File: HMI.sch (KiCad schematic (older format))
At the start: 48 parts, among them J34 Display, J35 SPI Interface, J36 I2C Interface, J37 LED4, J38 LED3, J39 Key 3, J40 Key 4, J41 Key 1, J42 Key 2, J43 Encoder, Q18 2N7002K, Q19 2N7002K, U11 74HC245

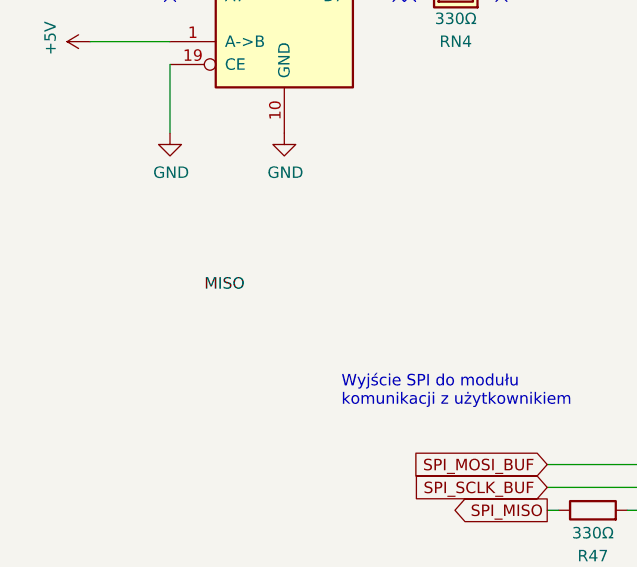
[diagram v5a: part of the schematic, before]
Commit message: Test points, start power plane routing, little change on schematic
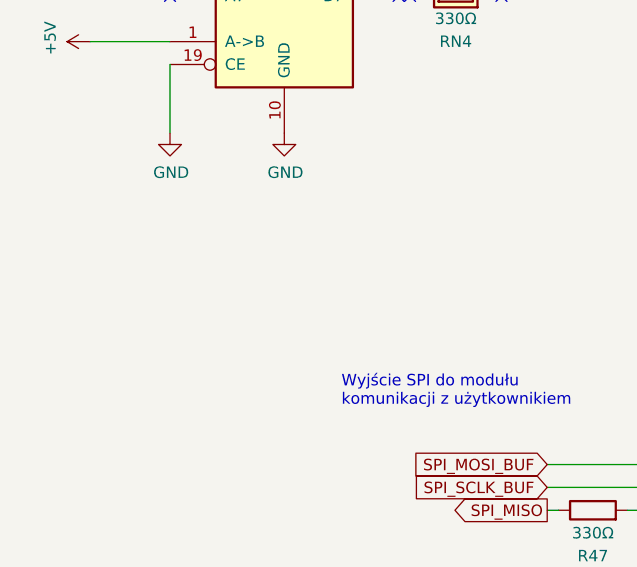
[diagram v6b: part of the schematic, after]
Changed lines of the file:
@@
 Wire Wire Line
 	3850 4700 3850 4900
-Text Label 1750 3650 0    50   ~ 0
-MISO
 $Comp
 L power:GND #PWR?

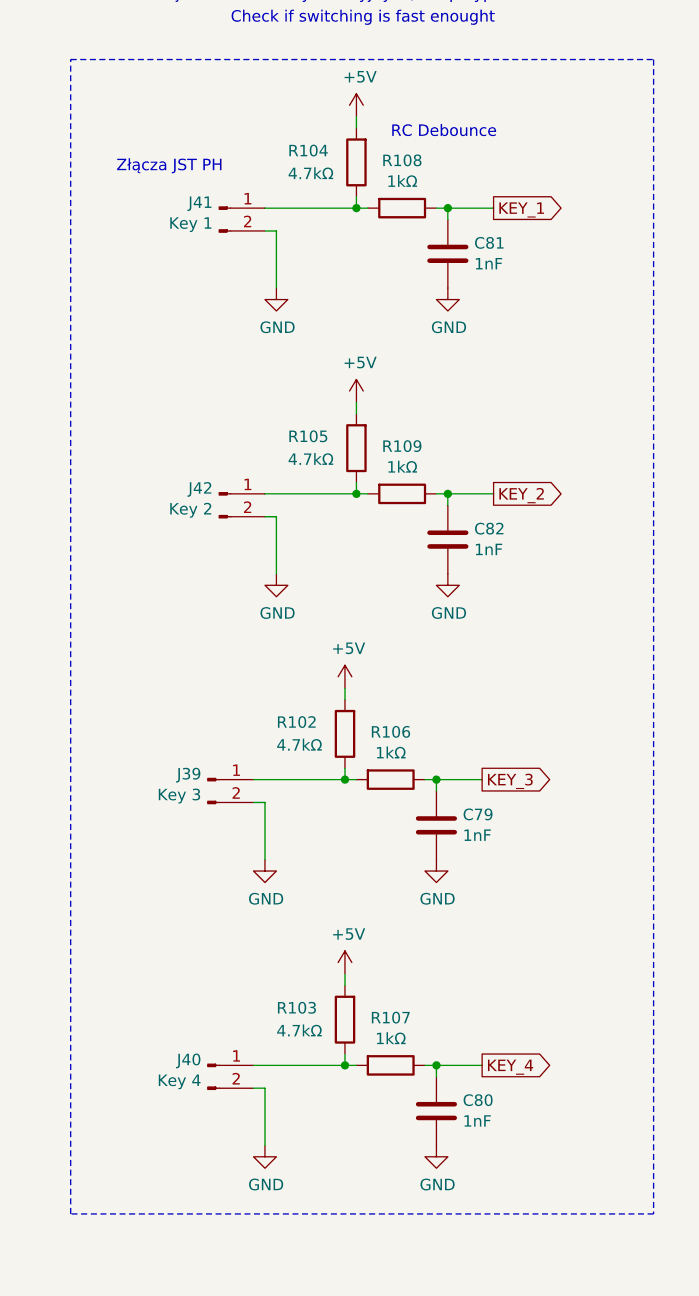
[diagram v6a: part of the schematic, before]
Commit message: Update elements value
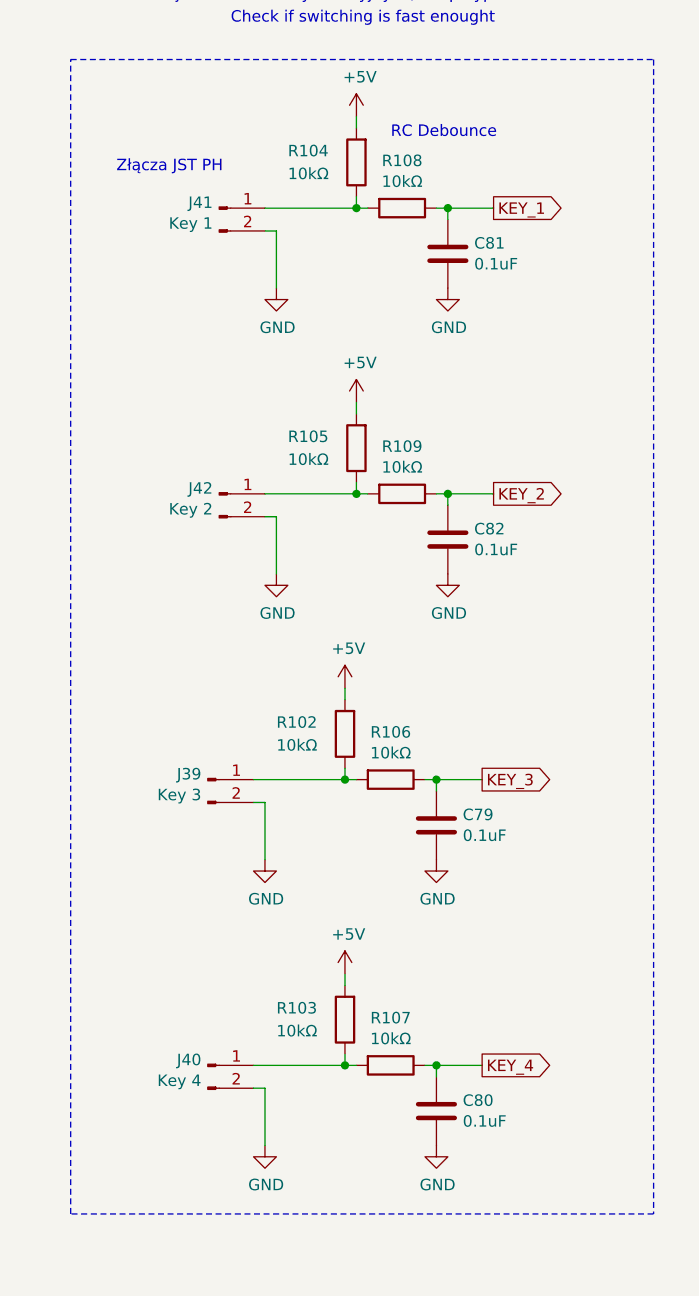
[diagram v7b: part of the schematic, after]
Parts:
- C79, C80, C81, C82: value 1nF -> 0.1uF
- R102, R103, R104, R105: value 4.7kΩ -> 10kΩ
- R106, R107, R108, R109: value 1kΩ -> 10kΩ
- R98, R99: Cena (none) -> 0.03185; Link (none) -> https://www.tme.eu/pl/details/smd0603-100r-1%25/rezystory-s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; Model (none) -> 0603SAF1000T5E; Opis (none) -> Rezystor: thick film; SMD; 0603; 100Ω; 0,1W; ±1%; -55÷155°C; Producent (none) -> ROYAL OHM; Typ (none) -> SMD
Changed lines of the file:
@@
 AR Path="/5E91D96F/5E1B03B6" Ref="C81"  Part="1"
 F 0 "C81" H 10015 1896 50  0000 L CNN
-F 1 "1nF" H 10015 1805 50  0000 L CNN
+F 1 "0.1uF" H 10015 1805 50  0000 L CNN
 F 2 "Capacitor_SMD:C_0603_1608Metric" H 9938 1700 50  0001 C CNN
 F 3 "~" H 9900 1850 50  0001 C CNN
@@
 AR Path="/5E91D96F/5E1B03BC" Ref="R104"  Part="1"
 F 0 "R104" H 9800 1400 50  0000 R CNN
-F 1 "4.7kΩ" H 9800 1500 50  0000 R CNN
+F 1 "10kΩ" H 9800 1500 50  0000 R CNN
 F 2 "Resistor_SMD:R_0603_1608Metric" V 9430 1450 50  0001 C CNN
 F 3 "~" H 9500 1450 50  0001 C CNN
@@
 AR Path="/5E91D96F/5E1B03C2" Ref="R108"  Part="1"
 F 0 "R108" V 9493 1650 50  0000 C CNN
-F 1 "1kΩ" V 9584 1650 50  0000 C CNN
+F 1 "10kΩ" V 9584 1650 50  0000 C CNN
 F 2 "Resistor_SMD:R_0603_1608Metric" V 9630 1650 50  0001 C CNN
 F 3 "~" H 9700 1650 50  0001 C CNN
@@
 AR Path="/5E91D96F/5E1B03E5" Ref="C82"  Part="1"
 F 0 "C82" H 10015 3146 50  0000 L CNN
-F 1 "1nF" H 10015 3055 50  0000 L CNN
+F 1 "0.1uF" H 10015 3055 50  0000 L CNN
 F 2 "Capacitor_SMD:C_0603_1608Metric" H 9938 2950 50  0001 C CNN
 F 3 "~" H 9900 3100 50  0001 C CNN
@@
 AR Path="/5E91D96F/5E1B03EB" Ref="R105"  Part="1"
 F 0 "R105" H 9800 2650 50  0000 R CNN
-F 1 "4.7kΩ" H 9800 2750 50  0000 R CNN
+F 1 "10kΩ" H 9800 2750 50  0000 R CNN
 F 2 "Resistor_SMD:R_0603_1608Metric" V 9430 2700 50  0001 C CNN
 F 3 "~" H 9500 2700 50  0001 C CNN
@@
 AR Path="/5E91D96F/5E1B03F1" Ref="R109"  Part="1"
 F 0 "R109" V 9493 2900 50  0000 C CNN
-F 1 "1kΩ" V 9584 2900 50  0000 C CNN
+F 1 "10kΩ" V 9584 2900 50  0000 C CNN
 F 2 "Resistor_SMD:R_0603_1608Metric" V 9630 2900 50  0001 C CNN
 F 3 "~" H 9700 2900 50  0001 C CNN
@@
 AR Path="/5E91D96F/5E1B0414" Ref="C79"  Part="1"
 F 0 "C79" H 9965 4396 50  0000 L CNN
-F 1 "1nF" H 9965 4305 50  0000 L CNN
+F 1 "0.1uF" H 9965 4305 50  0000 L CNN
 F 2 "Capacitor_SMD:C_0603_1608Metric" H 9888 4200 50  0001 C CNN
 F 3 "~" H 9850 4350 50  0001 C CNN
@@
 AR Path="/5E91D96F/5E1B041A" Ref="R102"  Part="1"
 F 0 "R102" H 9750 3900 50  0000 R CNN
-F 1 "4.7kΩ" H 9750 4000 50  0000 R CNN
+F 1 "10kΩ" H 9750 4000 50  0000 R CNN
 F 2 "Resistor_SMD:R_0603_1608Metric" V 9380 3950 50  0001 C CNN
 F 3 "~" H 9450 3950 50  0001 C CNN
@@
 AR Path="/5E91D96F/5E1B0420" Ref="R106"  Part="1"
 F 0 "R106" V 9443 4150 50  0000 C CNN
-F 1 "1kΩ" V 9534 4150 50  0000 C CNN
+F 1 "10kΩ" V 9534 4150 50  0000 C CNN
 F 2 "Resistor_SMD:R_0603_1608Metric" V 9580 4150 50  0001 C CNN
 F 3 "~" H 9650 4150 50  0001 C CNN
@@
 AR Path="/5E91D96F/5E1B0443" Ref="C80"  Part="1"
 F 0 "C80" H 9965 5646 50  0000 L CNN
-F 1 "1nF" H 9965 5555 50  0000 L CNN
+F 1 "0.1uF" H 9965 5555 50  0000 L CNN
 F 2 "Capacitor_SMD:C_0603_1608Metric" H 9888 5450 50  0001 C CNN
 F 3 "~" H 9850 5600 50  0001 C CNN
@@
 AR Path="/5E91D96F/5E1B0449" Ref="R103"  Part="1"
 F 0 "R103" H 9750 5150 50  0000 R CNN
-F 1 "4.7kΩ" H 9750 5250 50  0000 R CNN
+F 1 "10kΩ" H 9750 5250 50  0000 R CNN
 F 2 "Resistor_SMD:R_0603_1608Metric" V 9380 5200 50  0001 C CNN
 F 3 "~" H 9450 5200 50  0001 C CNN
@@
 AR Path="/5E91D96F/5E1B044F" Ref="R107"  Part="1"
 F 0 "R107" V 9443 5400 50  0000 C CNN
-F 1 "1kΩ" V 9534 5400 50  0000 C CNN
+F 1 "10kΩ" V 9534 5400 50  0000 C CNN
 F 2 "Resistor_SMD:R_0603_1608Metric" V 9580 5400 50  0001 C CNN
 F 3 "~" H 9650 5400 50  0001 C CNN
@@
 F 2 "Resistor_SMD:R_0603_1608Metric" V 5880 1700 50  0001 C CNN
 F 3 "~" H 5950 1700 50  0001 C CNN
+F 4 "0.03185" H 5950 1700 50  0001 C CNN "Cena"
+F 5 "https://www.tme.eu/pl/details/smd0603-100r-1%25/rezystory-smd-0603/royal-ohm/0603saf1000t5e/" H 5950 1700 50  0001 C CNN "Link"
+F 6 "0603SAF1000T5E" H 5950 1700 50  0001 C CNN "Model"
+F 7 "Rezystor: thick film; SMD; 0603; 100Ω; 0,1W; ±1%; -55÷155°C" H 5950 1700 50  0001 C CNN "Opis"
+F 8 "ROYAL OHM" H 5950 1700 50  0001 C CNN "Producent"
+F 9 "SMD" H 5950 1700 50  0001 C CNN "Typ"
 	1    5950 1700
 	0    -1   -1   0
@@
 F 2 "Resistor_SMD:R_0603_1608Metric" V 5880 2900 50  0001 C CNN
 F 3 "~" H 5950 2900 50  0001 C CNN
+F 4 "0.03185" H 5950 2900 50  0001 C CNN "Cena"
+F 5 "https://www.tme.eu/pl/details/smd0603-100r-1%25/rezystory-smd-0603/royal-ohm/0603saf1000t5e/" H 5950 2900 50  0001 C CNN "Link"
+F 6 "0603SAF1000T5E" H 5950 2900 50  0001 C CNN "Model"
+F 7 "Rezystor: thick film; SMD; 0603; 100Ω; 0,1W; ±1%; -55÷155°C" H 5950 2900 50  0001 C CNN "Opis"
+F 8 "ROYAL OHM" H 5950 2900 50  0001 C CNN "Producent"
+F 9 "SMD" H 5950 2900 50  0001 C CNN "Typ"
 	1    5950 2900
 	0    -1   -1   0

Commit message: Updated BOM on schematics
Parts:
- C78: Cena 0.05982 -> 0.07894; Link (none) -> https://www.tme.eu/pl/details/cl10b104kb8nnnc/kondensatory-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; Model CL10B104KB8NNNC -> CL10B104KB8NNNC; Opis (none) -> Kondensator: ceramiczny; MLCC; 100nF; 50V; X7R; ±10%; SMD; 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
- C79, C80, C81, C82: Cena 0.05563 -> 0.07894; Dielektryk (none) -> X7R; Link https://www.tme.eu/pl/details/cl10b102kb8nnnc/kondensatory-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 -> https://www.tme.eu/pl/details/cl10b104kb8nnnc/kondensatory-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; Model CL10B102KB8NNNC -> CL10B104KB8NNNC; Napięcie (none) -> 50V; Opis Kondensator: ceramiczny; MLCC; 1nF; 50V; X7R; ±10%; SMD; 06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 -> Kondensator: ceramiczny; MLCC; 100nF; 50V; X7R; ±10%; SMD; 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
- C85, C86: Cena 0.05563 -> 0.05269; Dielektryk (none) -> X7R; Link (none) -> https://www.tme.eu/pl/details/vj0603y103kxacw1bc/kondensato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; Model (none) -> VJ0603Y103KXACW1BC; Napięcie (none) -> 50V; Opis (none) -> Kondensator: ceramiczny; MLCC; 10nF; 50V; X7R; ±10%; SMD; 0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; Producent (none) -> VISHAY
- R100, R101, R47: Link (none) -> https://www.tme.eu/pl/details/smd0603-330r-1%25/rezystory-s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; Model (none) -> 0603SAF3300T5E; Opis (none) -> Rezystor: thick film; SMD; 0603; 330Ω; 0,1W; ±1%; -55÷155°C; Producent (none) -> ROYAL OHM
- R96, R97: Cena (none) -> 0.1; Link (none) -> https://www.tme.eu/pl/details/crcw060320r0fktabc/rezystory-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; Model (none) -> CRCW060320R0FKTABC; Opis (none) -> Rezystor: thick film; SMD; 0603; 20Ω; 0,1W; ±1%; -55÷155°C; Producent (none) -> VISHAY
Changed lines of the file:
@@
 F 2 "Capacitor_SMD:C_0603_1608Metric" H 9938 1700 50  0001 C CNN
 F 3 "~" H 9900 1850 50  0001 C CNN
-F 4 "0.05563" H 9900 1850 50  0001 C CNN "Cena"
-F 5 "https://www.tme.eu/pl/details/cl10b102kb8nnnc/kondensatory-mlcc-smd-0603/samsung/" H 9900 1850 50  0001 C CNN "Link"
-F 6 "CL10B102KB8NNNC" H 9900 1850 50  0001 C CNN "Model"
-F 7 "Kondensator: ceramiczny; MLCC; 1nF; 50V; X7R; ±10%; SMD; 0603" H 9900 1850 50  0001 C CNN "Opis"
+F 4 "0.07894" H 9900 1850 50  0001 C CNN "Cena"
+F 5 "https://www.tme.eu/pl/details/cl10b104kb8nnnc/kondensatory-mlcc-smd-0603/samsung/" H 9900 1850 50  0001 C CNN "Link"
+F 6 "CL10B104KB8NNNC" H 9900 1850 50  0001 C CNN "Model"
+F 7 "Kondensator: ceramiczny; MLCC; 100nF; 50V; X7R; ±10%; SMD; 0603" H 9900 1850 50  0001 C CNN "Opis"
 F 8 "SAMSUNG" H 9900 1850 50  0001 C CNN "Producent"
 F 9 "SMD" H 9900 1850 50  0001 C CNN "Typ"
+F 10 "X7R" H 9900 1850 50  0001 C CNN "Dielektryk"
+F 11 "50V" H 9900 1850 50  0001 C CNN "Napięcie"
 	1    9900 1850
 	1    0    0    -1
@@
 F 2 "Capacitor_SMD:C_0603_1608Metric" H 9938 2950 50  0001 C CNN
 F 3 "~" H 9900 3100 50  0001 C CNN
-F 4 "0.05563" H 9900 3100 50  0001 C CNN "Cena"
-F 5 "https://www.tme.eu/pl/details/cl10b102kb8nnnc/kondensatory-mlcc-smd-0603/samsung/" H 9900 3100 50  0001 C CNN "Link"
-F 6 "CL10B102KB8NNNC" H 9900 3100 50  0001 C CNN "Model"
-F 7 "Kondensator: ceramiczny; MLCC; 1nF; 50V; X7R; ±10%; SMD; 0603" H 9900 3100 50  0001 C CNN "Opis"
+F 4 "0.07894" H 9900 3100 50  0001 C CNN "Cena"
+F 5 "https://www.tme.eu/pl/details/cl10b104kb8nnnc/kondensatory-mlcc-smd-0603/samsung/" H 9900 3100 50  0001 C CNN "Link"
+F 6 "CL10B104KB8NNNC" H 9900 3100 50  0001 C CNN "Model"
+F 7 "Kondensator: ceramiczny; MLCC; 100nF; 50V; X7R; ±10%; SMD; 0603" H 9900 3100 50  0001 C CNN "Opis"
 F 8 "SAMSUNG" H 9900 3100 50  0001 C CNN "Producent"
 F 9 "SMD" H 9900 3100 50  0001 C CNN "Typ"
+F 10 "X7R" H 9900 3100 50  0001 C CNN "Dielektryk"
+F 11 "50V" H 9900 3100 50  0001 C CNN "Napięcie"
 	1    9900 3100
 	1    0    0    -1
@@
 F 2 "Capacitor_SMD:C_0603_1608Metric" H 9888 4200 50  0001 C CNN
 F 3 "~" H 9850 4350 50  0001 C CNN
-F 4 "0.05563" H 9850 4350 50  0001 C CNN "Cena"
-F 5 "https://www.tme.eu/pl/details/cl10b102kb8nnnc/kondensatory-mlcc-smd-0603/samsung/" H 9850 4350 50  0001 C CNN "Link"
-F 6 "CL10B102KB8NNNC" H 9850 4350 50  0001 C CNN "Model"
-F 7 "Kondensator: ceramiczny; MLCC; 1nF; 50V; X7R; ±10%; SMD; 0603" H 9850 4350 50  0001 C CNN "Opis"
+F 4 "0.07894" H 9850 4350 50  0001 C CNN "Cena"
+F 5 "https://www.tme.eu/pl/details/cl10b104kb8nnnc/kondensatory-mlcc-smd-0603/samsung/" H 9850 4350 50  0001 C CNN "Link"
+F 6 "CL10B104KB8NNNC" H 9850 4350 50  0001 C CNN "Model"
+F 7 "Kondensator: ceramiczny; MLCC; 100nF; 50V; X7R; ±10%; SMD; 0603" H 9850 4350 50  0001 C CNN "Opis"
 F 8 "SAMSUNG" H 9850 4350 50  0001 C CNN "Producent"
 F 9 "SMD" H 9850 4350 50  0001 C CNN "Typ"
+F 10 "X7R" H 9850 4350 50  0001 C CNN "Dielektryk"
+F 11 "50V" H 9850 4350 50  0001 C CNN "Napięcie"
 	1    9850 4350
 	1    0    0    -1
@@
 F 2 "Capacitor_SMD:C_0603_1608Metric" H 9888 5450 50  0001 C CNN
 F 3 "~" H 9850 5600 50  0001 C CNN
-F 4 "0.05563" H 9850 5600 50  0001 C CNN "Cena"
-F 5 "https://www.tme.eu/pl/details/cl10b102kb8nnnc/kondensatory-mlcc-smd-0603/samsung/" H 9850 5600 50  0001 C CNN "Link"
-F 6 "CL10B102KB8NNNC" H 9850 5600 50  0001 C CNN "Model"
-F 7 "Kondensator: ceramiczny; MLCC; 1nF; 50V; X7R; ±10%; SMD; 0603" H 9850 5600 50  0001 C CNN "Opis"
+F 4 "0.07894" H 9850 5600 50  0001 C CNN "Cena"
+F 5 "https://www.tme.eu/pl/details/cl10b104kb8nnnc/kondensatory-mlcc-smd-0603/samsung/" H 9850 5600 50  0001 C CNN "Link"
+F 6 "CL10B104KB8NNNC" H 9850 5600 50  0001 C CNN "Model"
+F 7 "Kondensator: ceramiczny; MLCC; 100nF; 50V; X7R; ±10%; SMD; 0603" H 9850 5600 50  0001 C CNN "Opis"
 F 8 "SAMSUNG" H 9850 5600 50  0001 C CNN "Producent"
 F 9 "SMD" H 9850 5600 50  0001 C CNN "Typ"
+F 10 "X7R" H 9850 5600 50  0001 C CNN "Dielektryk"
+F 11 "50V" H 9850 5600 50  0001 C CNN "Napięcie"
 	1    9850 5600
 	1    0    0    -1
@@
 F 4 "0.04651" H 6350 1300 50  0001 C CNN "Cena"
 F 5 "SMD" H 6350 1300 50  0001 C CNN "Typ"
+F 6 "https://www.tme.eu/pl/details/smd0603-330r-1%25/rezystory-smd-0603/royal-ohm/0603saf3300t5e/" H 6350 1300 50  0001 C CNN "Link"
+F 7 "0603SAF3300T5E" H 6350 1300 50  0001 C CNN "Model"
+F 8 "Rezystor: thick film; SMD; 0603; 330Ω; 0,1W; ±1%; -55÷155°C" H 6350 1300 50  0001 C CNN "Opis"
+F 9 "ROYAL OHM" H 6350 1300 50  0001 C CNN "Producent"
 	1    6350 1300
 	0    1    1    0
@@
 F 4 "0.04651" H 6350 2500 50  0001 C CNN "Cena"
 F 5 "SMD" H 6350 2500 50  0001 C CNN "Typ"
+F 6 "https://www.tme.eu/pl/details/smd0603-330r-1%25/rezystory-smd-0603/royal-ohm/0603saf3300t5e/" H 6350 2500 50  0001 C CNN "Link"
+F 7 "0603SAF3300T5E" H 6350 2500 50  0001 C CNN "Model"
+F 8 "Rezystor: thick film; SMD; 0603; 330Ω; 0,1W; ±1%; -55÷155°C" H 6350 2500 50  0001 C CNN "Opis"
+F 9 "ROYAL OHM" H 6350 2500 50  0001 C CNN "Producent"
 	1    6350 2500
 	0    1    1    0
@@
 F 2 "Capacitor_SMD:C_0603_1608Metric" H 2288 950 50  0001 C CNN
 F 3 "~" H 2250 1100 50  0001 C CNN
-F 4 "0.05982" H 2250 1100 50  0001 C CNN "Cena"
+F 4 "0.07894" H 2250 1100 50  0001 C CNN "Cena"
 F 5 "X7R" H 2250 1100 50  0001 C CNN "Dielektryk"
-F 6 "CL10B104KB8NNNC " H 2250 1100 50  0001 C CNN "Model"
+F 6 "CL10B104KB8NNNC" H 2250 1100 50  0001 C CNN "Model"
 F 7 "50V" H 2250 1100 50  0001 C CNN "Napięcie"
 F 8 "SAMSUNG" H 2250 1100 50  0001 C CNN "Producent"
 F 9 "10%" H 2250 1100 50  0001 C CNN "Tolerancja"
 F 10 "SMD" H 2250 1100 50  0001 C CNN "Typ"
+F 11 "https://www.tme.eu/pl/details/cl10b104kb8nnnc/kondensatory-mlcc-smd-0603/samsung/" H 2250 1100 50  0001 C CNN "Link"
+F 12 "Kondensator: ceramiczny; MLCC; 100nF; 50V; X7R; ±10%; SMD; 0603" H 2250 1100 50  0001 C CNN "Opis"
 	1    2250 1100
 	1    0    0    -1
@@
 F 2 "Resistor_SMD:R_0603_1608Metric" V 3480 6200 50  0001 C CNN
 F 3 "~" H 3550 6200 50  0001 C CNN
-F 4 "" H 3550 6200 50  0001 C CNN "Cena"
-F 5 "" H 3550 6200 50  0001 C CNN "Link"
-F 6 "" H 3550 6200 50  0001 C CNN "Model"
-F 7 "" H 3550 6200 50  0001 C CNN "Opis"
-F 8 "" H 3550 6200 50  0001 C CNN "Producent"
+F 4 "0.1" H 3550 6200 50  0001 C CNN "Cena"
+F 5 "https://www.tme.eu/pl/details/crcw060320r0fktabc/rezystory-smd-0603/vishay/" H 3550 6200 50  0001 C CNN "Link"
+F 6 "CRCW060320R0FKTABC" H 3550 6200 50  0001 C CNN "Model"
+F 7 "Rezystor: thick film; SMD; 0603; 20Ω; 0,1W; ±1%; -55÷155°C" H 3550 6200 50  0001 C CNN "Opis"
+F 8 "VISHAY" H 3550 6200 50  0001 C CNN "Producent"
 F 9 "SMD" H 3550 6200 50  0001 C CNN "Typ"
 	1    3550 6200
@@
 F 2 "Resistor_SMD:R_0603_1608Metric" V 3480 6400 50  0001 C CNN
 F 3 "~" H 3550 6400 50  0001 C CNN
-F 4 "" H 3550 6400 50  0001 C CNN "Cena"
-F 5 "" H 3550 6400 50  0001 C CNN "Link"
-F 6 "" H 3550 6400 50  0001 C CNN "Model"
-F 7 "" H 3550 6400 50  0001 C CNN "Opis"
-F 8 "" H 3550 6400 50  0001 C CNN "Producent"
+F 4 "0.1" H 3550 6400 50  0001 C CNN "Cena"
+F 5 "https://www.tme.eu/pl/details/crcw060320r0fktabc/rezystory-smd-0603/vishay/" H 3550 6400 50  0001 C CNN "Link"
+F 6 "CRCW060320R0FKTABC" H 3550 6400 50  0001 C CNN "Model"
+F 7 "Rezystor: thick film; SMD; 0603; 20Ω; 0,1W; ±1%; -55÷155°C" H 3550 6400 50  0001 C CNN "Opis"
+F 8 "VISHAY" H 3550 6400 50  0001 C CNN "Producent"
 F 9 "SMD" H 3550 6400 50  0001 C CNN "Typ"
 	1    3550 6400
@@
 F 2 "Capacitor_SMD:C_0603_1608Metric" H 7288 4900 50  0001 C CNN
 F 3 "~" H 7250 5050 50  0001 C CNN
-F 4 "0.05563" H 7250 5050 50  0001 C CNN "Cena"
-F 5 "" H 7250 5050 50  0001 C CNN "Link"
-F 6 "" H 7250 5050 50  0001 C CNN "Model"
-F 7 "" H 7250 5050 50  0001 C CNN "Opis"
-F 8 "" H 7250 5050 50  0001 C CNN "Producent"
+F 4 "0.05269" H 7250 5050 50  0001 C CNN "Cena"
+F 5 "https://www.tme.eu/pl/details/vj0603y103kxacw1bc/kondensatory-mlcc-smd-0603/vishay/" H 7250 5050 50  0001 C CNN "Link"
+F 6 "VJ0603Y103KXACW1BC" H 7250 5050 50  0001 C CNN "Model"
+F 7 "Kondensator: ceramiczny; MLCC; 10nF; 50V; X7R; ±10%; SMD; 0603" H 7250 5050 50  0001 C CNN "Opis"
+F 8 "VISHAY" H 7250 5050 50  0001 C CNN "Producent"
 F 9 "SMD" H 7250 5050 50  0001 C CNN "Typ"
+F 10 "X7R" H 7250 5050 50  0001 C CNN "Dielektryk"
+F 11 "50V" H 7250 5050 50  0001 C CNN "Napięcie"
 	1    7250 5050
 	1    0    0    -1
@@
 F 2 "Capacitor_SMD:C_0603_1608Metric" H 6838 4900 50  0001 C CNN
 F 3 "~" H 6800 5050 50  0001 C CNN
-F 4 "0.05563" H 6800 5050 50  0001 C CNN "Cena"
-F 5 "" H 6800 5050 50  0001 C CNN "Link"
-F 6 "" H 6800 5050 50  0001 C CNN "Model"
-F 7 "" H 6800 5050 50  0001 C CNN "Opis"
-F 8 "" H 6800 5050 50  0001 C CNN "Producent"
+F 4 "0.05269" H 6800 5050 50  0001 C CNN "Cena"
+F 5 "https://www.tme.eu/pl/details/vj0603y103kxacw1bc/kondensatory-mlcc-smd-0603/vishay/" H 6800 5050 50  0001 C CNN "Link"
+F 6 "VJ0603Y103KXACW1BC" H 6800 5050 50  0001 C CNN "Model"
+F 7 "Kondensator: ceramiczny; MLCC; 10nF; 50V; X7R; ±10%; SMD; 0603" H 6800 5050 50  0001 C CNN "Opis"
+F 8 "VISHAY" H 6800 5050 50  0001 C CNN "Producent"
 F 9 "SMD" H 6800 5050 50  0001 C CNN "Typ"
+F 10 "X7R" H 6800 5050 50  0001 C CNN "Dielektryk"
+F 11 "50V" H 6800 5050 50  0001 C CNN "Napięcie"
 	1    6800 5050
 	1    0    0    -1
@@
 F 4 "0.04651" H 3450 4600 50  0001 C CNN "Cena"
 F 5 "SMD" H 3450 4600 50  0001 C CNN "Typ"
+F 6 "https://www.tme.eu/pl/details/smd0603-330r-1%25/rezystory-smd-0603/royal-ohm/0603saf3300t5e/" H 3450 4600 50  0001 C CNN "Link"
+F 7 "0603SAF3300T5E" H 3450 4600 50  0001 C CNN "Model"
+F 8 "Rezystor: thick film; SMD; 0603; 330Ω; 0,1W; ±1%; -55÷155°C" H 3450 4600 50  0001 C CNN "Opis"
+F 9 "ROYAL OHM" H 3450 4600 50  0001 C CNN "Producent"
 	1    3450 4600
 	0    -1   -1   0
